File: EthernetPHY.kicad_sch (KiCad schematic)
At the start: 37 parts, among them J6 Ethernet, SW6 SW_Push, U5 DP83826IRHBR, Y2 25MHz

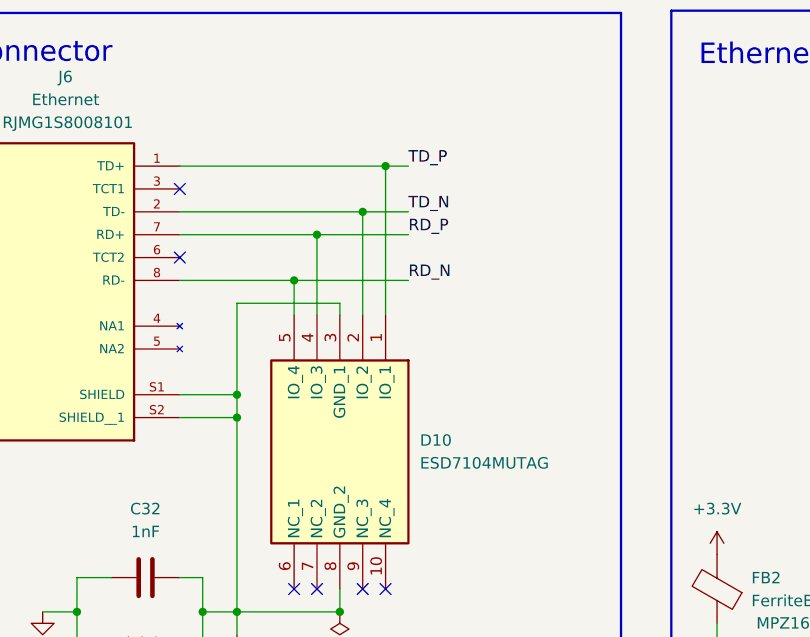
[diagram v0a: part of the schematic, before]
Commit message: Alternate MPNs added
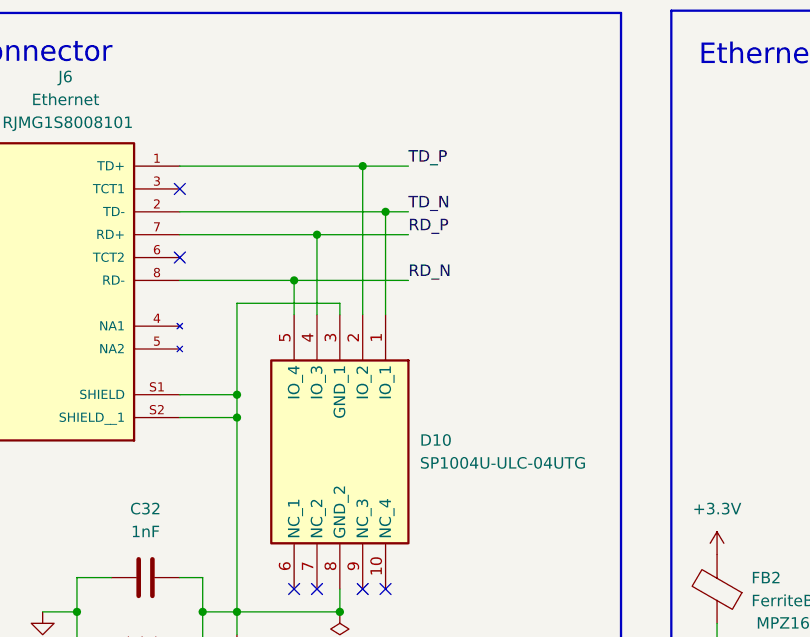
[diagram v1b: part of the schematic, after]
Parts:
- D10: value ESD7104MUTAG -> SP1004U-ULC-04UTG; MPN ESD7104MUTAG -> SP1004U-ULC-04UTG; Manufacturer_Name onsemi -> Littelfuse; Mouser Part Number 863-ESD7104MUTAG -> (none); Mouser Price/Stock https://www.mouser.co.uk/ProductDetail/onsemi/ESD7104MUTAG?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 -> (none)
- FB2: MPN MPZ1608S601 -> MPZ1608S601ATA00; Manufacturer_Part_Number (none) -> MPZ1608S601
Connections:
- net TD_N: now also D10.1 (IO_1); no longer D10.2 (IO_2)
- net TD_P: now also D10.2 (IO_2); no longer D10.1 (IO_1)
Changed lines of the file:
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@@
 	)
 	(junction
-		(at 72.39 36.83)
+		(at 152.4 128.27)
 		(diameter 0)
 		(color 0 0 0 0)
 	)
 	(junction
-		(at 152.4 128.27)
+		(at 74.93 36.83)
 		(diameter 0)
 		(color 0 0 0 0)
@@
 	)
 	(junction
+		(at 72.39 31.75)
+		(diameter 0)
+		(color 0 0 0 0)
+	)
+	(junction
 		(at 27.94 142.24)
 		(diameter 0)
@@
 	)
 	(junction
-		(at 74.93 31.75)
-		(diameter 0)
-		(color 0 0 0 0)
-	)
-	(junction
 		(at 58.42 81.28)
 		(diameter 0)
@@
 	(wire
 		(pts
-			(xy 72.39 36.83) (xy 72.39 48.26)
-		)
-		(stroke
-			(width 0)
-			(type default)
-		)
-	)
-	(wire
-		(pts
 			(xy 186.69 39.37) (xy 190.5 39.37)
 		)
@@
 	(wire
 		(pts
-			(xy 52.07 36.83) (xy 72.39 36.83)
-		)
-		(stroke
-			(width 0)
-			(type default)
-		)
-	)
-	(wire
-		(pts
 			(xy 163.83 81.28) (xy 152.4 81.28)
 		)
@@
 	(wire
 		(pts
-			(xy 74.93 31.75) (xy 74.93 48.26)
-		)
-		(stroke
-			(width 0)
-			(type default)
-		)
-	)
-	(wire
-		(pts
 			(xy 146.05 105.41) (xy 144.78 105.41)
 		)
@@
 	(wire
 		(pts
+			(xy 74.93 36.83) (xy 74.93 48.26)
+		)
+		(stroke
+			(width 0)
+			(type default)
+		)
+	)
+	(wire
+		(pts
 			(xy 58.42 57.15) (xy 58.42 59.69)
 		)
@@
 	(wire
 		(pts
-			(xy 72.39 36.83) (xy 77.47 36.83)
+			(xy 52.07 36.83) (xy 74.93 36.83)
 		)
 		(stroke
@@
 	(wire
 		(pts
+			(xy 74.93 36.83) (xy 77.47 36.83)
+		)
+		(stroke
+			(width 0)
+			(type default)
+		)
+	)
+	(wire
+		(pts
 			(xy 233.68 66.04) (xy 233.68 69.85)
 		)
@@
 	(wire
 		(pts
-			(xy 52.07 31.75) (xy 74.93 31.75)
-		)
-		(stroke
-			(width 0)
-			(type default)
-		)
-	)
-	(wire
-		(pts
 			(xy 229.87 99.06) (xy 234.95 99.06)
 		)
@@
 	(wire
 		(pts
+			(xy 72.39 31.75) (xy 72.39 48.26)
+		)
+		(stroke
+			(width 0)
+			(type default)
+		)
+	)
+	(wire
+		(pts
 			(xy 160.02 116.84) (xy 160.02 110.49)
 		)
@@
 	(wire
 		(pts
+			(xy 72.39 31.75) (xy 77.47 31.75)
+		)
+		(stroke
+			(width 0)
+			(type default)
+		)
+	)
+	(wire
+		(pts
 			(xy 52.07 59.69) (xy 58.42 59.69)
 		)
@@
 	(wire
 		(pts
-			(xy 74.93 31.75) (xy 77.47 31.75)
+			(xy 52.07 31.75) (xy 72.39 31.75)
 		)
 		(stroke
@@
 			)
 		)
-		(property "Value" "ESD7104MUTAG"
+		(property "Value" "SP1004U-ULC-04UTG"
 			(at 78.74 64.7699 90)
 			(effects
@@
 			)
 		)
-		(property "Datasheet" "https://www.onsemi.com/pub/Collateral/ESD7104-D.PDF"
+		(property "Datasheet" "https://www.littelfuse.com/assetdocs/ultra-low-capacitance-diode-arrays-series-datasheet?assetguid=03876E90-1979-448E-B2EE-6071EF500868"
 			(at -119.99 74.93 0)
 			(effects
@@
 			)
 		)
-		(property "Description" "TVS DIODE 5VWM 10VC 10UDFN"
+		(property "Description" "ESD Protection Diodes / TVS Diodes 5V .2pF 20kV 4CH"
 			(at 74.93 48.26 0)
 			(effects
@@
 			)
 		)
-		(property "Mouser Part Number" "863-ESD7104MUTAG"
-			(at -419.99 74.93 0)
-			(effects
-				(font
-					(size 1.27 1.27)
-				)
-				(justify left top)
-				(hide yes)
-			)
-		)
-		(property "Mouser Price/Stock" "https://www.mouser.co.uk/ProductDetail/onsemi/ESD7104MUTAG?qs=8nbDJddAfDXw%2Fvxmx%252Bz6Hg%3D%3D"
-			(at -519.99 74.93 0)
-			(effects
-				(font
-					(size 1.27 1.27)
-				)
-				(justify left top)
-				(hide yes)
-			)
-		)
-		(property "Manufacturer_Name" "onsemi"
+		(property "Manufacturer_Name" "Littelfuse"
 			(at -619.99 74.93 0)
 			(effects
@@
 			)
 		)
-		(property "MPN" "ESD7104MUTAG"
+		(property "MPN" "SP1004U-ULC-04UTG"
 			(at -719.99 74.93 0)
 			(effects
@@
 			)
 		)
-		(property "MPN" "MPZ1608S601"
+		(property "MPN" "MPZ1608S601ATA00"
 			(at 122.428 82.55 0)
 			(effects
@@
 					(color 0 132 132 1)
 				)
+				(hide yes)
 			)
 		)
@@
 			)
 		)
-		(property "Manufacturer_Part_Number" ""
-			(at 111.76 78.74 0)
+		(property "Manufacturer_Part_Number" "MPZ1608S601"
+			(at 122.428 82.55 0)
 			(effects
 				(font
 					(size 1.27 1.27)
+					(color 0 132 132 1)
 				)
-				(hide yes)
 			)
 		)

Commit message: SV's comments
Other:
- note added: "Add TPs"
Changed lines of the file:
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@@
+	)
+	(rectangle
+		(start 233.68 30.48)
+		(end 250.19 44.45)
+		(stroke
+			(width 0)
+			(type default)
+		)
+		(fill
+			(type none)
+		)
 	)
 	(rectangle
@@
 			)
 		)
+	)
+	(text "Add TPs"
+		(exclude_from_sim no)
+		(at 240.284 35.052 0)
+		(effects
+			(font
+				(size 1.27 1.27)
+				(color 255 15 3 1)
+			)
+		)

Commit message: All comments addressed
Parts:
- C32: footprint Capacitor_SMD:C_0603_1608Metric -> Capacitor_SMD:C_1206_3216Metric; MPN GRM188R72A102KA01D -> CC1206KKX7RDBB102
- SW6: Alternate MPN (none) -> PTS645SH50SMTR92 LFS; MPN PTS645SK50SMTR92 LFS -> SWT0310-043016GSA
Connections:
- net RD_N: now also D10.1 (IO_1); no longer D10.5 (IO_4)
- net RD_P: now also D10.2 (IO_2); no longer D10.4 (IO_3)
- net TD_N: now also D10.4 (IO_3); no longer D10.1 (IO_1)
- net TD_P: now also D10.5 (IO_4); no longer D10.2 (IO_2)
